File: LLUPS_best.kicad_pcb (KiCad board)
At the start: 2 copper layers, 140 x 90 mm, 39 parts, among them J1 USB_C, J2 Output, J3 Debug, Q1 FS8205A, U1 USBLC6-2SC6, U2 BQ24072, U3 HY2113-KB5B, U4 MT3608, U5 AP2112K-3.3, U6 LN61CN3302MR-G

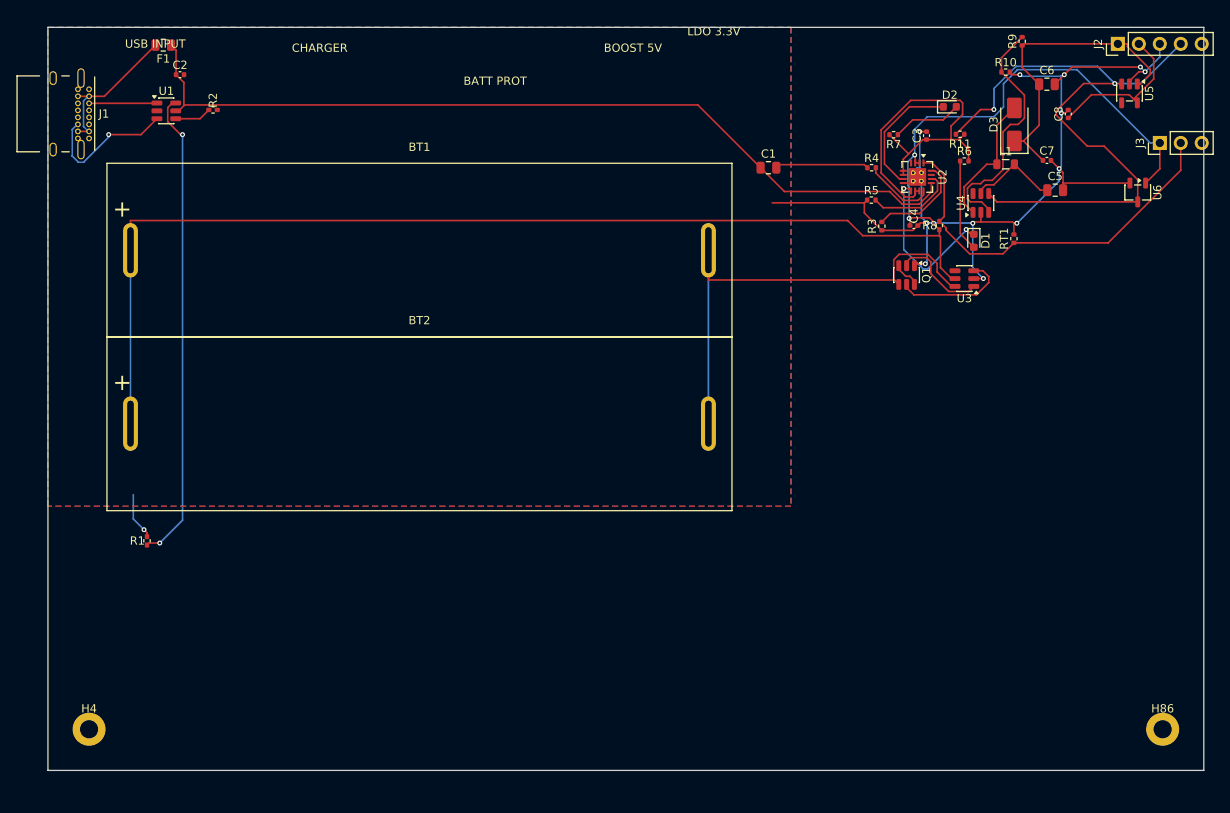
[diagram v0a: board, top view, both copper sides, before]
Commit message: Fix placement, start/stop lifecycle, frame gen, battery overlap, and silkscreen labels
Placement fixes:
- Randomize edge component positions instead of deterministic pinning
- Fix _clamp_pads_to_board bug (separate shift tracking + max_y typo)
- Add THT detection and backside layer assignment for large through-hole parts
- Enable board size search with 70/30 shrink bias
- Increase area weight from 5% to 10%

Start/stop lifecycle:
- FreeRouting subprocess uses process groups (start_new_session + killpg)
- ExperimentRunner uses process groups for clean termination
- SIGTERM handler in autoexperiment creates stop.now for graceful shutdown
- Write 'stopping' phase to status JSON, cancel futures mid-batch
- Singleton ExperimentRunner on AppState (no lost Popen references)
- GUI button state machine: Start/Stop/Force Kill with stopping spinner

Frame generation:
- Log warnings instead of silently swallowing snapshot_pcb errors
- Pre-flight check for kicad-cli and magick availability
- Remove dead round_num_local variable

Battery courtyard overlap:
- Split BT1/BT2 zones to bottom-left/bottom-right
- Resolve locked-locked overlaps by moving smaller component
- 15pt penalty for large component overlaps (vs 5pt normal)

Silkscreen group labels:
- Regenerate group labels on final output PCB via add_group_labels()
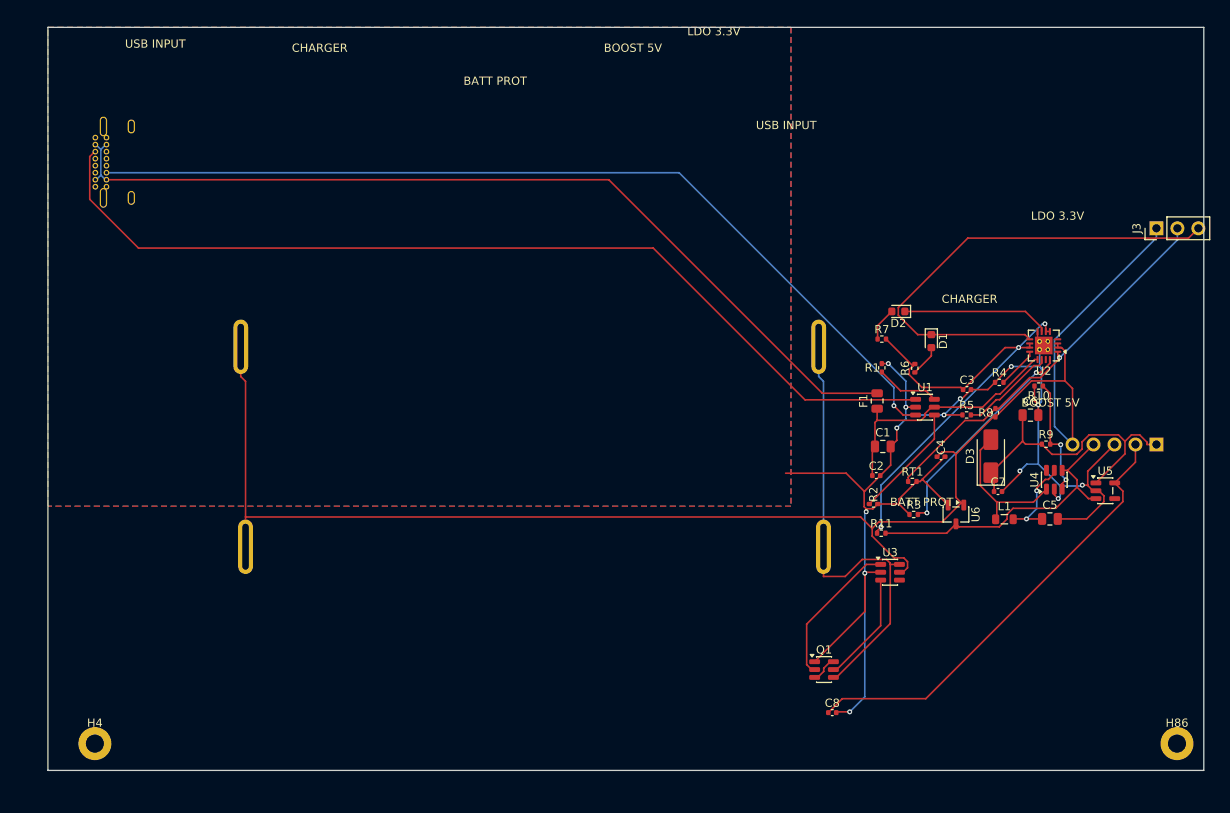
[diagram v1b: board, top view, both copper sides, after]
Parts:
- BT1, BT2, J1, J2: moved to B.Cu
- moved U1 98.6 mm to (106.2, 46.0)
- moved C2 97.3 mm to (100.3, 54.3)
- moved F1 96.6 mm to (100.4, 45.3), turned to 90 degrees
- moved R2 93.2 mm to (100.0, 57.7)
- moved R1 91.4 mm to (101.0, 41.2)
- moved C8 77.9 mm to (95.0, 83.0), turned to 0 degrees
- moved R11 49.3 mm to (100.9, 61.3), turned to 0 degrees
- moved R9 48.9 mm to (120.9, 50.5), turned to 0 degrees
- moved Q1 48.8 mm to (94.0, 77.8), turned to 0 degrees
- moved J2 48.7 mm to (134.3, 50.5)
- moved U5 48.2 mm to (128.1, 56.1), turned to 0 degrees
- moved U6 44.8 mm to (110.0, 59.0)
- moved L1 43.0 mm to (115.8, 59.6)
- moved C7 40.5 mm to (115.1, 56.2)
- moved D3 40.3 mm to (114.2, 51.9)
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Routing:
- net Net-(J1-CC1): track 8.23 -> 116.2 mm
- net Net-(J1-CC2): track 17.1 -> 111.5 mm
- net Net-(F1-Pad2): track 18.2 -> 110.8 mm
- net /VBUS: track 106.4 -> 31.0 mm
- net Net-(R1-Pad1): track 57.6 -> 7.73 mm, vias 2 -> 0
- net /EN: track 79.1 -> 36.6 mm, vias 2 -> 0
- net /CHG_N: track 20.1 -> 58.4 mm, vias 2 -> 0
- net /3V3: track 18.4 -> 54.6 mm
- net GND: track 142.2 -> 169.6 mm
- net Net-(U4-FB): track 29.9 -> 14.5 mm, vias 0 -> 2
- net /VSYS: track 45.0 -> 59.6 mm, vias 0 -> 3
- net Net-(U2-ISET): track 12.0 -> 26.2 mm, vias 0 -> 2
- net Net-(R2-Pad1): track 4.45 -> 14.0 mm
- net Net-(D1-A): track 11.1 -> 3.83 mm
- net Net-(Q1A-G): track 11.6 -> 18.1 mm
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
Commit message: Fix 10 experiment issues: zones, DRC, edge compliance, gates, retry
- Strip pre-existing F.Cu/B.Cu zones via subprocess before routing
- Patch DSN smd_smd clearance from 0.05mm to match KiCad 0.2mm rule
- Fix edge_compliance scoring margin (3mm -> edge_margin + 2.0)
- Lower placement gates: min_placement 30->20, courtyard 50->10
- Add FreeRouting retry on crash (2 attempts, reduced passes)
- Zone refill after routing, before DRC
- ensure_gnd_zone runs in subprocess (avoids SWIG corruption)
- Elite archive stale min_placement_score override
- SWIG output parsing fix for strip_zones

Results: score 90.25->92.17, DRC 114->45 (-60%), 0 crashes
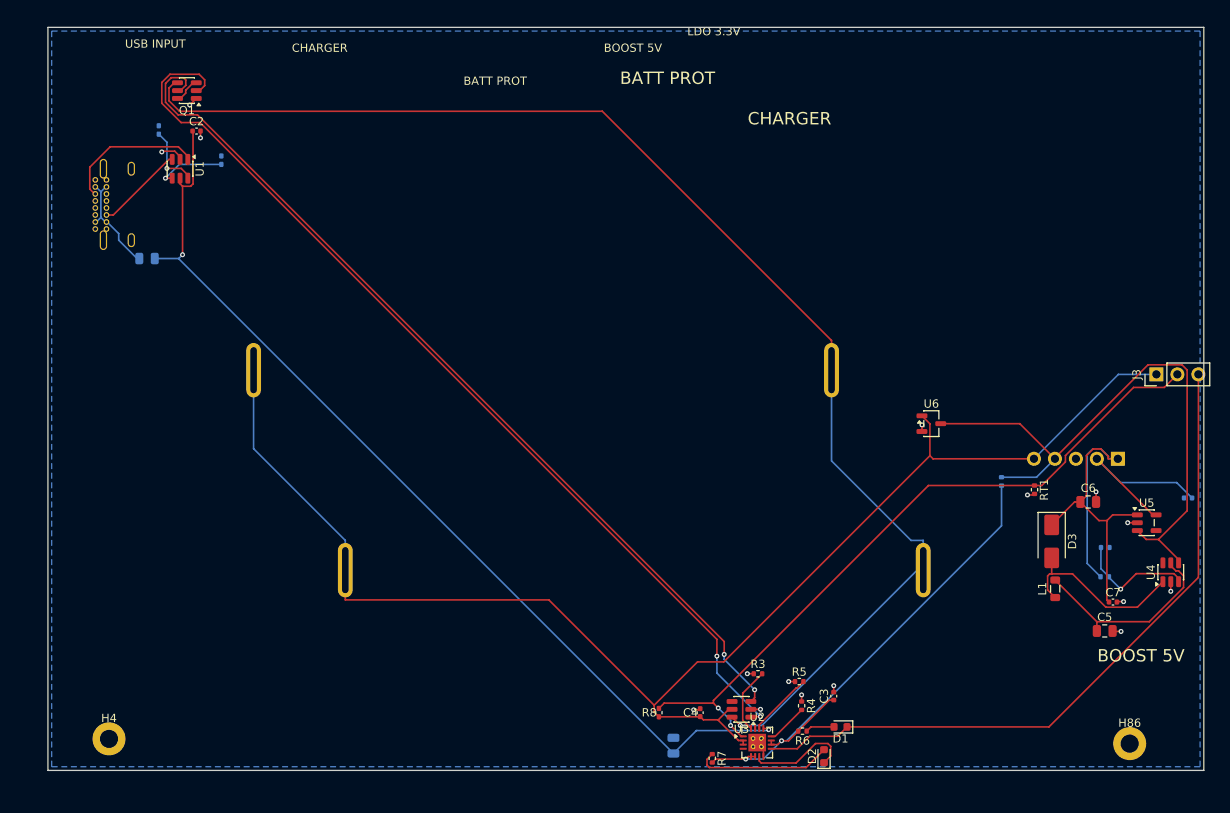
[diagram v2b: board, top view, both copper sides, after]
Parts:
- C1, C8, F1, R1, R10, R11, R2, R9: moved to B.Cu
- moved Q1 104.3 mm to (16.8, 7.66), turned to 180 degrees
- moved U1 94.7 mm to (16.0, 17.1), turned to -90 degrees
- moved C2 92.3 mm to (18.0, 12.6)
- moved R1 92.2 mm to (13.4, 12.4)
- moved F1 90.1 mm to (12.0, 28.0), turned to 180 degrees
- moved R2 89.3 mm to (21.0, 16.1), turned to 90 degrees
- moved U2 59.3 mm to (85.9, 86.6), turned to 0 degrees
- moved R7 54.8 mm to (80.5, 88.5), turned to -90 degrees
- moved D2 54.6 mm to (94.0, 88.3), turned to 90 degrees
- moved R8 54.6 mm to (74.0, 83.0)
- moved C8 50.3 mm to (138.1, 57.0), turned to 180 degrees
- moved D1 48.0 mm to (96.0, 84.7), turned to 180 degrees
- moved R6 46.0 mm to (91.4, 85.2), turned to 180 degrees
- moved R4 45.9 mm to (91.3, 82.2), turned to -90 degrees
- moved C1 44.2 mm to (75.8, 87.0), turned to 90 degrees
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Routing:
- net GND: track 169.6 -> 19.1 mm, vias 13 -> 16
- net /CELL_NEG: track 55.2 -> 160.1 mm, vias 0 -> 1
- net Net-(J1-CC2): track 111.5 -> 10.7 mm, vias 1 -> 0
- net Net-(Q1A-G): track 18.1 -> 117.2 mm, vias 0 -> 2
- net Net-(J1-CC1): track 116.2 -> 17.3 mm
- net Net-(F1-Pad2): track 110.8 -> 13.0 mm
- net Net-(Q1B-G): track 13.4 -> 110.8 mm, vias 0 -> 2
- net /VBUS: track 31.0 -> 119.0 mm, vias 0 -> 2
- net /NTC_SENSE: track 47.4 -> 85.8 mm, vias 1 -> 2
- net /EN: track 36.6 -> 72.9 mm
- net /3V3: track 54.6 -> 23.5 mm
- net /CHG_N: track 58.4 -> 84.9 mm
- net /VBAT: track 193.0 -> 173.9 mm
- net Net-(U2-ISET): track 26.2 -> 8.03 mm, vias 2 -> 0
- net /5V: track 37.1 -> 53.6 mm
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- removed copper zone on F.Cu, net GND

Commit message: fix: rotation convention (CW), layer flip pad mirroring, hard pad-containment gate
- Fix _update_pad_positions to use KiCad's rotation convention
  (x'=x*cos+y*sin, y'=-x*sin+y*cos) instead of CCW math convention
- Fix _best_rotation_for_edge: delta = current - desired (not desired - current)
- Fix _optimize_rotations and _place_clusters early rotation to use CW formula
- Mirror pad X offsets in _assign_layers when flipping components to B.Cu
  to match KiCad Flip() behavior
- Reorder solve(): assign layers BEFORE edge pinning so pinned positions
  account for flipped pad geometry
- Add _clamp_pads_to_board after _restore_pinned_positions (defense in depth)
- Add hard pads_outside_board gate in pipeline: reject placement if ANY
  pad is outside the board boundary (zero tolerance)
- Add pads_outside_board count to PlacementEngine return dict

Score: 92.1, 26/26 nets routed, 0 pads outside board (verified by KiCad)
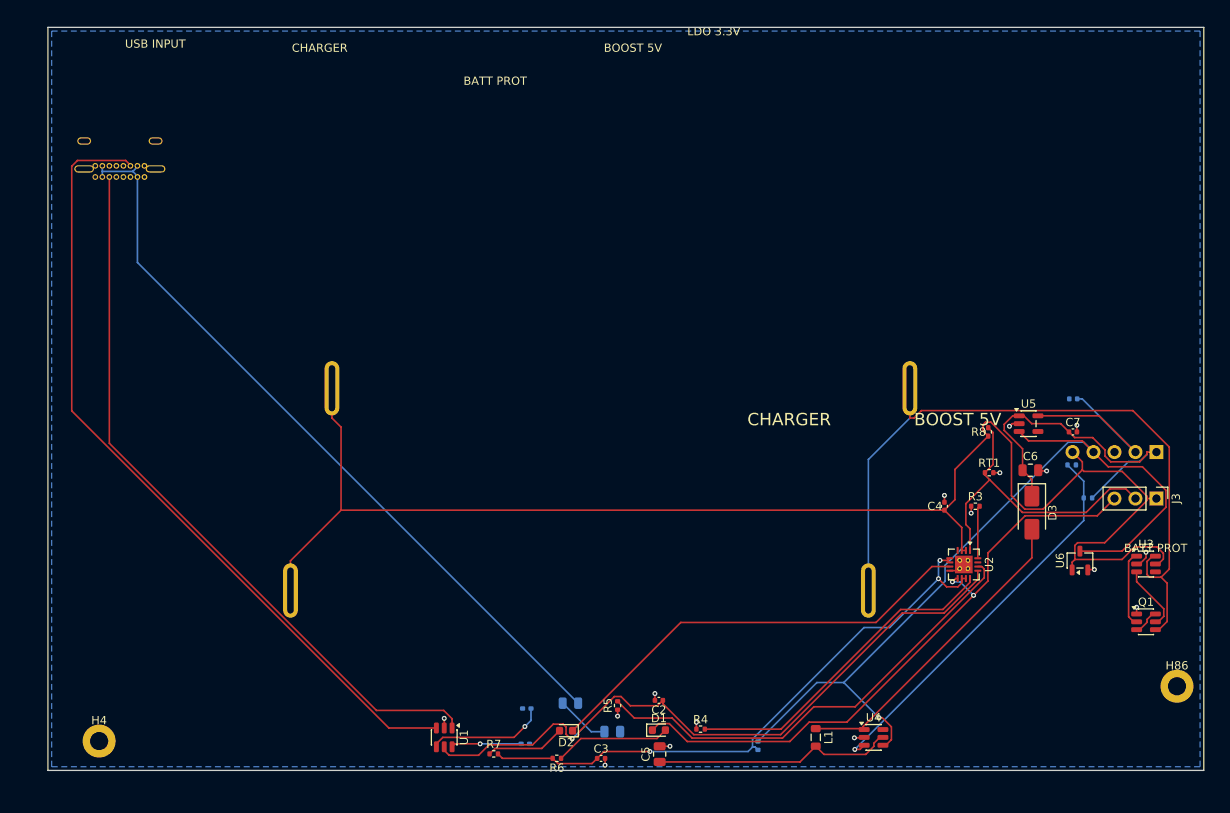
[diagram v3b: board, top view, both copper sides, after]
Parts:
- moved Q1 132.8 mm to (133.0, 72.0), turned to 0 degrees
- moved C2 88.8 mm to (74.0, 81.5), turned to 180 degrees
- moved R1 86.6 mm to (57.8, 86.8), turned to 0 degrees
- moved R2 76.0 mm to (58.0, 82.5), turned to 180 degrees
- moved U1 75.9 mm to (48.0, 86.0)
- moved F1 74.4 mm to (63.3, 81.9), turned to 0 degrees
- moved C5 55.9 mm to (74.1, 88.0), turned to 90 degrees
- moved R8 52.4 mm to (113.9, 49.0)
- moved U3 52.1 mm to (133.0, 65.0), turned to 0 degrees
- moved R11 43.5 mm to (86.0, 87.0)
- moved U4 41.2 mm to (100.0, 86.0), turned to 0 degrees
- moved C4 38.7 mm to (108.6, 58.0)
- moved L1 34.1 mm to (93.0, 86.0), turned to -90 degrees
- moved R3 33.2 mm to (112.3, 58.0)
- moved U2 33.0 mm to (110.9, 65.1), turned to -90 degrees
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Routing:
- net Net-(Q1A-G): track 117.2 -> 9.17 mm, vias 2 -> 0
- net Net-(Q1B-G): track 110.8 -> 8.04 mm, vias 2 -> 0
- net Net-(J1-CC2): track 10.7 -> 97.4 mm
- net Net-(F1-Pad2): track 13.0 -> 92.7 mm
- net Net-(J1-CC1): track 17.3 -> 88.7 mm
- net /CELL_NEG: track 160.1 -> 92.2 mm, vias 1 -> 0
- net Net-(U2-TMR): track 7.97 -> 56.2 mm
- net /NTC_SENSE: track 85.8 -> 38.1 mm, vias 2 -> 0
- net Net-(D2-K): track 12.7 -> 53.9 mm
- net Net-(U2-ILIM): track 5.01 -> 40.0 mm
- net Net-(U4-FB): track 14.5 -> 48.1 mm
- net /EN: track 72.9 -> 103.5 mm, vias 0 -> 1
- net /VBUS: track 119.0 -> 90.7 mm, vias 2 -> 1
- net Net-(D3-A): track 22.0 -> 38.5 mm
- net /5V: track 53.6 -> 42.6 mm
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
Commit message: fix: connector orientation using body center instead of footprint origin
_best_rotation_for_edge() measured pad centroid from footprint origin,
which for connectors like USB-C is at a corner pad. The centroid angle
(~22°) snapped to 0° delta, leaving the connector facing wrong.

Fix: add body_center (courtyard bbox center) to Component data model
and use it as reference. From body center, pad centroid is at 270°
(perpendicular to opening), correctly producing rotation 270° for
left-edge connectors.

Also rewrote orientation_check.py to validate facing dynamically
using body-center-to-pad-centroid angle instead of hard-coded rotation
table.
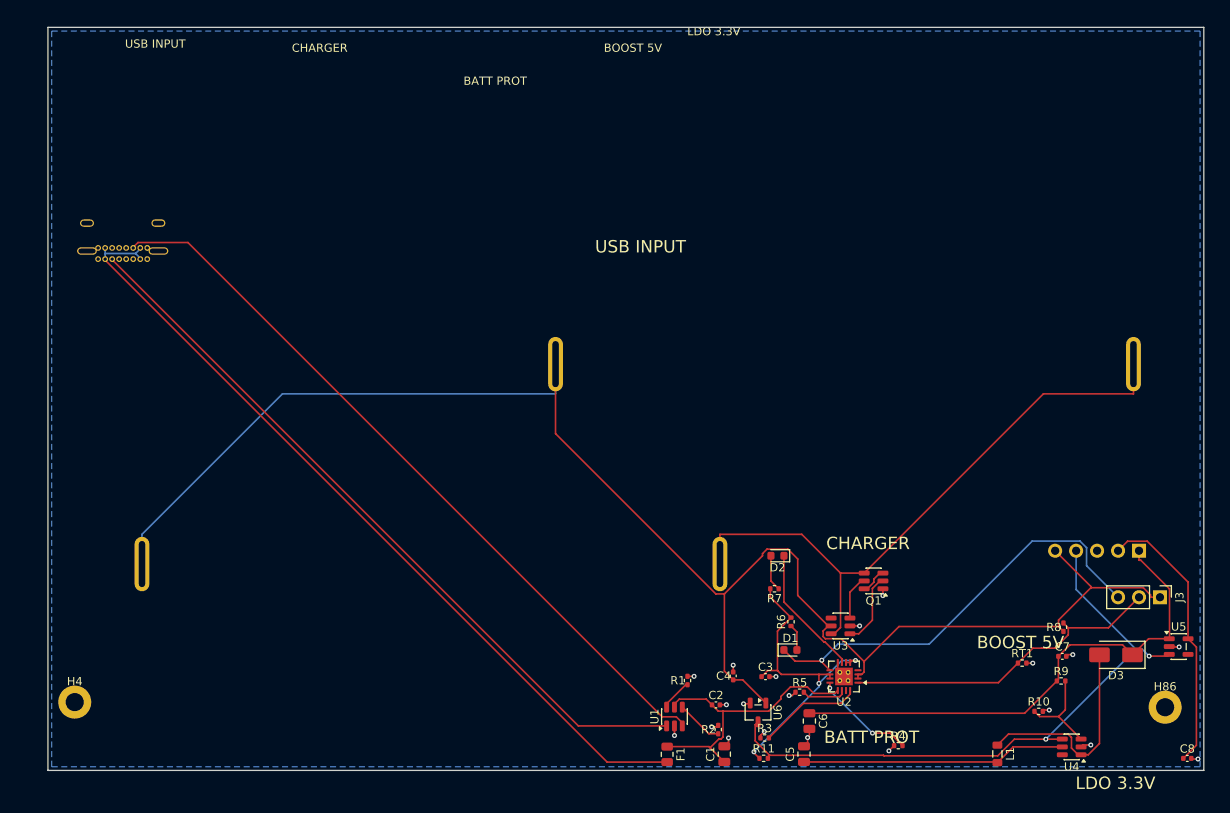
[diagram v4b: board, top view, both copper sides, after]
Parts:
- C1, C8, F1, R1, R10, R11, R2, R9: moved to F.Cu
- moved C8 45.7 mm to (138.0, 88.5), turned to 0 degrees
- moved U6 43.1 mm to (86.0, 83.0), turned to -90 degrees
- moved C6 40.5 mm to (92.2, 84.0), turned to -90 degrees
- moved R7 39.4 mm to (88.0, 68.0), turned to 180 degrees
- moved R3 37.9 mm to (86.8, 86.1)
- moved U3 37.8 mm to (96.0, 72.5), turned to 180 degrees
- moved Q1 33.4 mm to (100.0, 67.0), turned to 180 degrees
- moved D2 33.2 mm to (88.4, 64.0)
- moved R6 32.8 mm to (90.0, 72.0), turned to 90 degrees
- moved C4 32.8 mm to (83.0, 78.6)
- moved U5 32.6 mm to (137.0, 75.0)
- moved R10 30.1 mm to (120.0, 82.8)
- moved U1 28.0 mm to (75.9, 83.5), turned to 90 degrees
- moved BT1 27.2 mm to (96.5, 40.8)
- moved C7 27.2 mm to (122.9, 76.2)
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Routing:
- net /VBUS: track 90.7 -> 35.8 mm, vias 1 -> 0
- net Net-(U2-TMR): track 56.2 -> 5.41 mm
- net Net-(D2-K): track 53.9 -> 15.9 mm
- net Net-(U4-FB): track 48.1 -> 11.7 mm, vias 1 -> 0
- net /VSYS: track 72.9 -> 41.4 mm
- net Net-(U2-ILIM): track 40.0 -> 12.5 mm, vias 0 -> 2
- net /EN: track 103.5 -> 76.5 mm, vias 1 -> 2
- net /CHG_N: track 75.4 -> 52.7 mm, vias 2 -> 1
- net /5V: track 42.6 -> 62.3 mm
- net /CELL_NEG: track 92.2 -> 76.3 mm
- net /VBAT: track 183.0 -> 197.1 mm
- net Net-(D3-A): track 38.5 -> 26.0 mm
- net Net-(D1-A): track 14.1 -> 3.20 mm
- net /3V3: track 23.4 -> 33.4 mm
- net Net-(R2-Pad1): track 14.4 -> 5.69 mm, vias 1 -> 0
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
